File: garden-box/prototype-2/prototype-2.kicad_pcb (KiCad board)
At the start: 2 copper layers, 230 x 150 mm, 23 parts, among them J1 USB_A, J2 Conn_01x03_Male, J3 Conn_01x04_Male, J4 Screw_Terminal_01x02, J5 Screw_Terminal_01x02, J6 Screw_Terminal_01x02, K1 G6DN-1A-L_DC5, Q1 2N3904, T1 Transformer_1P_2S, U1 ESP32-POE

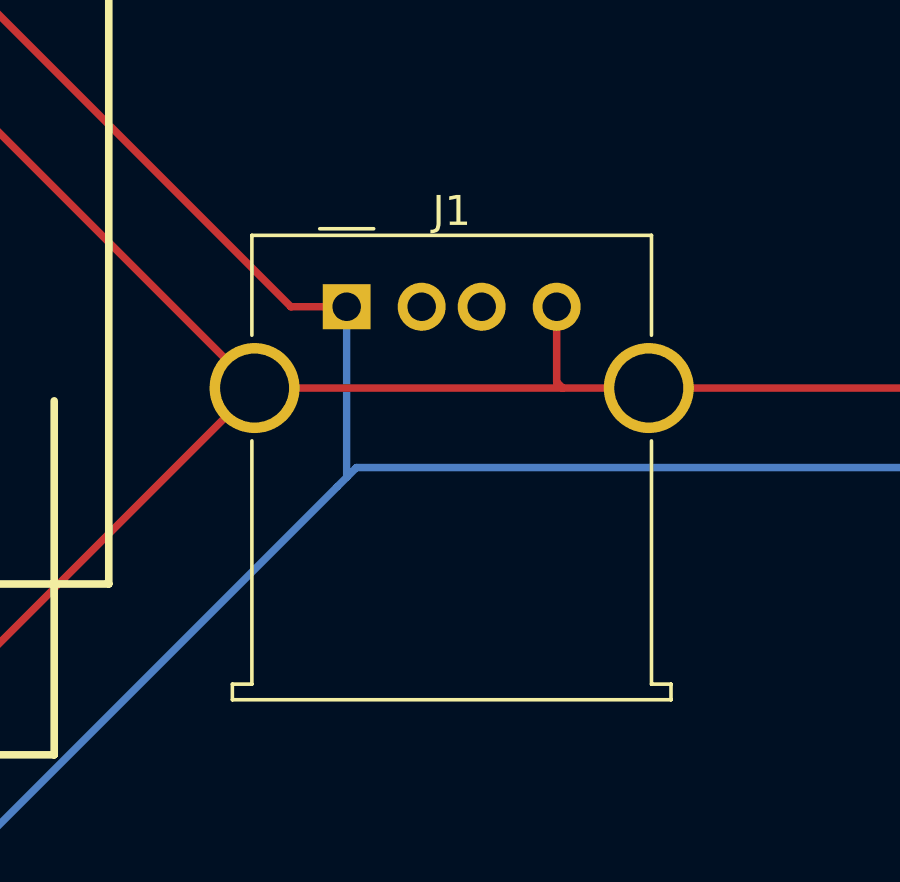
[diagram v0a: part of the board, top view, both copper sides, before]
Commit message: update usb connector
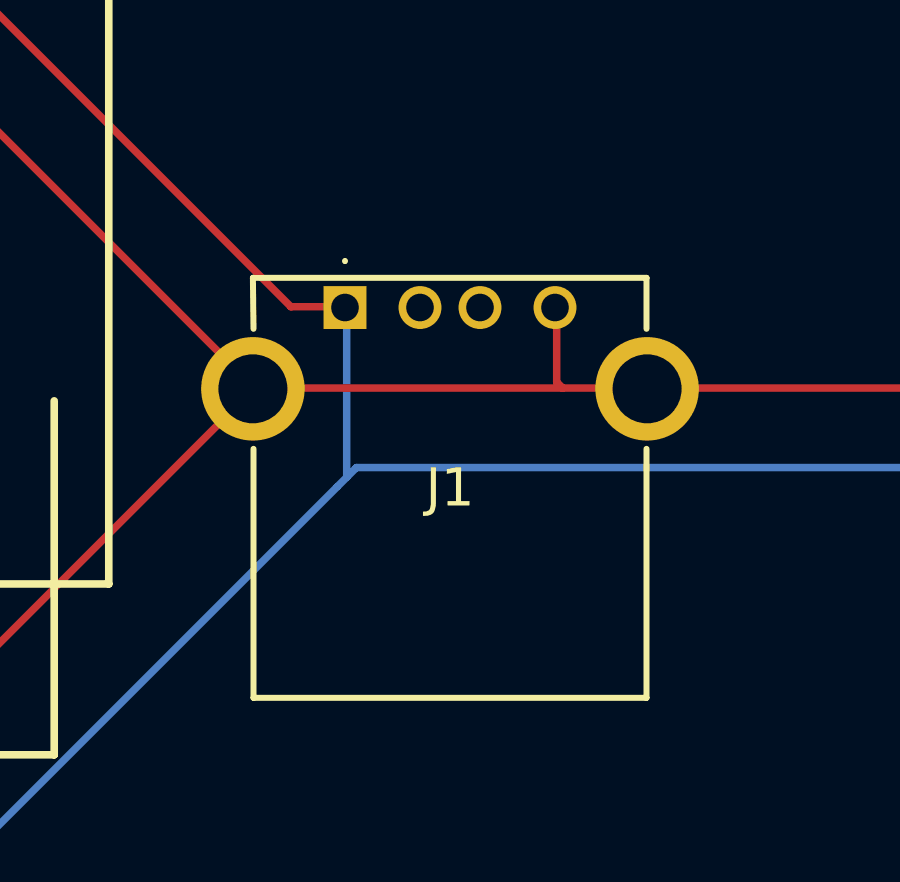
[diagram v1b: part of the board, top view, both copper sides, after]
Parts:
- J1: footprint Connector_USB:USB_A_Molex_67643_Horizontal -> rs-online:875200010BLF
- moved J1 0.06 mm to (159.0, 101.3)
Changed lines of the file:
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@@
-    )
-  )
-  (footprint "Connector_USB:USB_A_Molex_67643_Horizontal" (layer "F.Cu")
-    (at 159.06 101.32)
-    (descr "USB type A, Horizontal, https://www.molex.com/pdm_docs/sd/676433910_sd.pdf")
-    (tags "USB_A Female Connector receptacle")
-    (property "Sheetfile" "prototype-2.kicad_sch")
-    (property "Sheetname" "")
-    (attr through_hole)
-    (fp_text reference "J1" (at 3.5 -3.19) (layer "F.SilkS")
-      (effects (font (size 1 1) (thickness 0.15)))
-    )
-    (fp_text value "USB_A" (at 3.5 14.5) (layer "F.Fab")
-      (effects (font (size 1 1) (thickness 0.15)))
-    )
-    (fp_text user "${REFERENCE}" (at 3.5 3.7) (layer "F.Fab")
-      (effects (font (size 1 1) (thickness 0.15)))
-    )
-    (fp_line (start -3.16 -2.38) (end 10.16 -2.38) (layer "F.SilkS") (width 0.12))
-    (fp_line (start -3.81 12.58) (end -3.81 13.1) (layer "F.SilkS") (width 0.12))
-    (fp_line (start 10.16 4.47) (end 10.16 12.58) (layer "F.SilkS") (width 0.12))
-    (fp_line (start -0.9 -2.6) (end 0.9 -2.6) (layer "F.SilkS") (width 0.12))
-    (fp_line (start -3.16 12.58) (end -3.81 12.58) (layer "F.SilkS") (width 0.12))
-    (fp_line (start -3.16 -2.38) (end -3.16 0.95) (layer "F.SilkS") (width 0.12))
-    (fp_line (start 10.81 12.58) (end 10.16 12.58) (layer "F.SilkS") (width 0.12))
-    (fp_line (start 10.81 13.1) (end 10.81 12.58) (layer "F.SilkS") (width 0.12))
-    (fp_line (start -3.16 12.58) (end -3.16 4.47) (layer "F.SilkS") (width 0.12))
-    (fp_line (start -3.81 13.1) (end 10.81 13.1) (layer "F.SilkS") (width 0.12))
-    (fp_line (start 10.16 -2.38) (end 10.16 0.95) (layer "F.SilkS") (width 0.12))
-    (fp_line (start -4.2 13.49) (end 11.2 13.49) (layer "F.CrtYd") (width 0.05))
-    (fp_line (start -4.2 13.49) (end -4.2 12.19) (layer "F.CrtYd") (width 0.05))
-    (fp_line (start -4.2 12.19) (end -3.55 12.19) (layer "F.CrtYd") (width 0.05))
-    (fp_line (start 10.55 12.19) (end 10.55 4.66) (layer "F.CrtYd") (width 0.05))
-    (fp_line (start 11.2 13.49) (end 11.2 12.19) (layer "F.CrtYd") (width 0.05))
-    (fp_line (start 10.55 -2.77) (end 10.55 0.76) (layer "F.CrtYd") (width 0.05))
-    (fp_line (start 11.2 12.19) (end 10.55 12.19) (layer "F.CrtYd") (width 0.05))
-    (fp_line (start -3.55 -2.77) (end 10.55 -2.77) (layer "F.CrtYd") (width 0.05))
-    (fp_line (start -3.55 12.19) (end -3.55 4.66) (layer "F.CrtYd") (width 0.05))
-    (fp_line (start -3.55 -2.77) (end -3.55 0.76) (layer "F.CrtYd") (width 0.05))
-    (fp_arc (start -3.55 4.66) (mid -5.078208 2.71) (end -3.55 0.76) (layer "F.CrtYd") (width 0.05))
-    (fp_arc (start 10.55 0.76) (mid 12.078208 2.71) (end 10.55 4.66) (layer "F.CrtYd") (width 0.05))
-    (fp_line (start 10.7 12.69) (end 10.05 12.69) (layer "F.Fab") (width 0.1))
-    (fp_line (start -3.7 12.99) (end 10.7 12.99) (layer "F.Fab") (width 0.1))
-    (fp_line (start 10.7 12.99) (end 10.7 12.69) (layer "F.Fab") (width 0.1))
-    (fp_line (start -3.05 12.69) (end -3.05 -2.27) (layer "F.Fab") (width 0.1))
-    (fp_line (start 10.05 -2.27) (end 10.05 12.69) (layer "F.Fab") (width 0.1))
-    (fp_line (start -3.05 12.69) (end -3.7 12.69) (layer "F.Fab") (width 0.1))
-    (fp_line (start -1 -2.27) (end 0 -1.27) (layer "F.Fab") (width 0.1))
-    (fp_line (start -3.05 9.27) (end 10.05 9.27) (layer "F.Fab") (width 0.1))
-    (fp_line (start -3.7 12.69) (end -3.7 12.99) (layer "F.Fab") (width 0.1))
-    (fp_line (start 0 -1.27) (end 1 -2.27) (layer "F.Fab") (width 0.1))
-    (fp_line (start -3.05 -2.27) (end 10.05 -2.27) (layer "F.Fab") (width 0.1))
-    (pad "1" thru_hole rect locked (at 0 0) (size 1.6 1.5) (drill 0.95) (layers *.Cu *.Mask)
-      (net 3 "+5V") (pinfunction "VBUS") (pintype "power_in"))
-    (pad "2" thru_hole circle locked (at 2.5 0) (size 1.6 1.6) (drill 0.95) (layers *.Cu *.Mask)
-      (net 5 "unconnected-(J1-Pad2)") (pinfunction "D-") (pintype "bidirectional"))
-    (pad "3" thru_hole circle locked (at 4.5 0) (size 1.6 1.6) (drill 0.95) (layers *.Cu *.Mask)
-      (net 6 "unconnected-(J1-Pad3)") (pinfunction "D+") (pintype "bidirectional"))
-    (pad "4" thru_hole circle locked (at 7 0) (size 1.6 1.6) (drill 0.95) (layers *.Cu *.Mask)
-      (net 4 "GND") (pinfunction "GND") (pintype "power_in"))
-    (pad "5" thru_hole circle locked (at -3.07 2.71) (size 3 3) (drill 2.3) (layers *.Cu *.Mask)
-      (net 4 "GND") (pinfunction "Shield") (pintype "passive"))
-    (pad "5" thru_hole circle locked (at 10.07 2.71) (size 3 3) (drill 2.3) (layers *.Cu *.Mask)
-      (net 4 "GND") (pinfunction "Shield") (pintype "passive"))
-    (model "${KICAD6_3DMODEL_DIR}/Connector_USB.3dshapes/USB_A_Molex_67643_Horizontal.wrl"
-      (offset (xyz 0 0 0))
-      (scale (xyz 1 1 1))
-      (rotate (xyz 0 0 0))
     )
   )
@@
     )
   )
+  (footprint "rs-online:875200010BLF" (layer "F.Cu")
+    (at 159.004 101.346)
+    (descr "87520-0010BLF-4")
+    (tags "Connector")
+    (property "Sheetfile" "prototype-2.kicad_sch")
+    (property "Sheetname" "")
+    (attr through_hole)
+    (fp_text reference "J1" (at 3.5 6.01) (layer "F.SilkS")
+      (effects (font (size 1.27 1.27) (thickness 0.254)))
+    )
+    (fp_text value "USB_A" (at 3.5 6.01) (layer "F.SilkS") hide
+      (effects (font (size 1.27 1.27) (thickness 0.254)))
+    )
+    (fp_text user "${REFERENCE}" (at 3.5 6.01) (layer "F.Fab")
+      (effects (font (size 1.27 1.27) (thickness 0.254)))
+    )
+    (fp_line (start 10.05 4.71) (end 10.05 13.01) (layer "F.SilkS") (width 0.2))
+    (fp_line (start 0 -1.5) (end 0 -1.5) (layer "F.SilkS") (width 0.1))
+    (fp_line (start -3.05 0.71) (end -3.07 -0.99) (layer "F.SilkS") (width 0.2))
+    (fp_line (start 10.05 13.01) (end -3.05 13.01) (layer "F.SilkS") (width 0.2))
+    (fp_line (start -3.07 -0.99) (end 10.05 -0.99) (layer "F.SilkS") (width 0.2))
+    (fp_line (start -3.05 13.01) (end -3.05 4.71) (layer "F.SilkS") (width 0.2))
+    (fp_line (start 0 -1.6) (end 0 -1.6) (layer "F.SilkS") (width 0.1))
+    (fp_line (start 10.05 -0.99) (end 10.05 0.71) (layer "F.SilkS") (width 0.2))
+    (fp_arc (start 0 -1.5) (mid -0.05 -1.55) (end 0 -1.6) (layer "F.SilkS") (width 0.1))
+    (fp_arc (start 0 -1.6) (mid 0.05 -1.55) (end 0 -1.5) (layer "F.SilkS") (width 0.1))
+    (fp_line (start 12.795 14.01) (end -5.795 14.01) (layer "F.CrtYd") (width 0.1))
+    (fp_line (start -5.795 14.01) (end -5.795 -1.99) (layer "F.CrtYd") (width 0.1))
+    (fp_line (start -5.795 -1.99) (end 12.795 -1.99) (layer "F.CrtYd") (width 0.1))
+    (fp_line (start 12.795 -1.99) (end 12.795 14.01) (layer "F.CrtYd") (width 0.1))
+    (fp_line (start -3.05 13.01) (end 10.05 13.01) (layer "F.Fab") (width 0.1))
+    (fp_line (start 10.05 13.01) (end 10.05 -0.99) (layer "F.Fab") (width 0.1))
+    (fp_line (start 10.05 -0.99) (end -3.05 -0.99) (layer "F.Fab") (width 0.1))
+    (fp_line (start -3.05 -0.99) (end -3.05 13.01) (layer "F.Fab") (width 0.1))
+    (pad "1" thru_hole rect (at 0 0) (size 1.431 1.431) (drill 0.92) (layers *.Cu *.Mask)
+      (net 3 "+5V") (pinfunction "VBUS") (pintype "power_in"))
+    (pad "2" thru_hole circle (at 2.5 0) (size 1.431 1.431) (drill 0.92) (layers *.Cu *.Mask)
+      (net 5 "unconnected-(J1-Pad2)") (pinfunction "D-") (pintype "bidirectional"))
+    (pad "3" thru_hole circle (at 4.5 0) (size 1.431 1.431) (drill 0.92) (layers *.Cu *.Mask)
+      (net 6 "unconnected-(J1-Pad3)") (pinfunction "D+") (pintype "bidirectional"))
+    (pad "4" thru_hole circle (at 7 0) (size 1.431 1.431) (drill 0.92) (layers *.Cu *.Mask)
+      (net 4 "GND") (pinfunction "GND") (pintype "power_in"))
+    (pad "5" thru_hole circle (at 10.07 2.71) (size 3.45 3.45) (drill 2.3) (layers *.Cu *.Mask)
+      (net 4 "GND") (pinfunction "Shield") (pintype "passive"))
+    (pad "5" thru_hole circle (at -3.07 2.71) (size 3.45 3.45) (drill 2.3) (layers *.Cu *.Mask)
+      (net 4 "GND") (pinfunction "Shield") (pintype "passive"))
+    (model "87520-0010BLF.stp"
+      (offset (xyz 3.499999947 0.9899999947 3.449999996))
+      (scale (xyz 1 1 1))
+      (rotate (xyz -90 0 0))
+    )
+  )

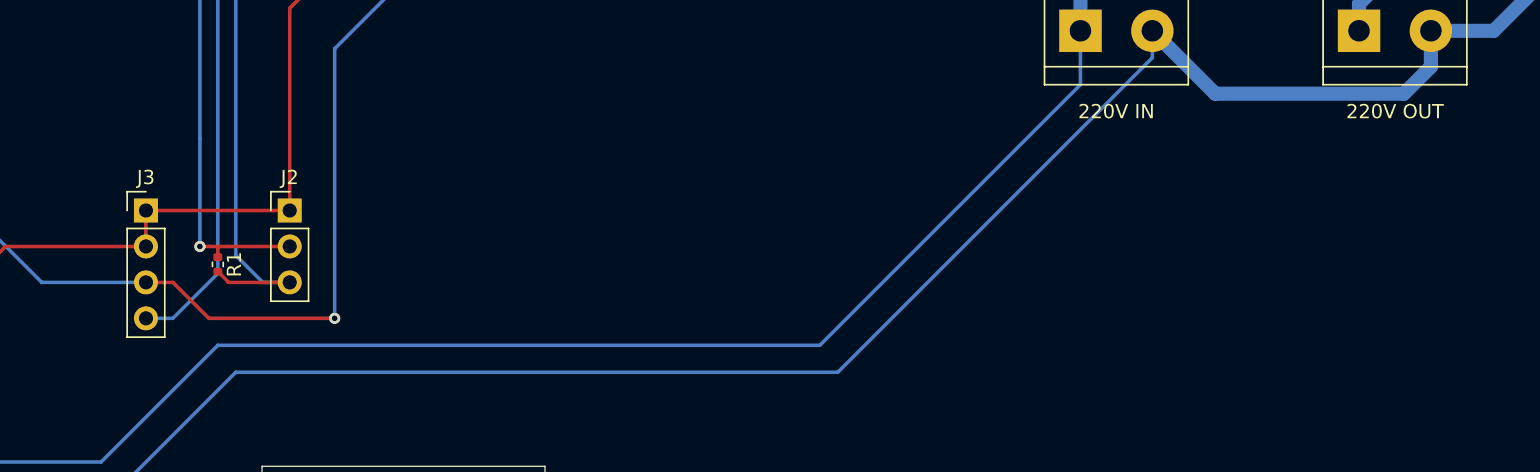
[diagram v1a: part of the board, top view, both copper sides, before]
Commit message: improve silkscreen
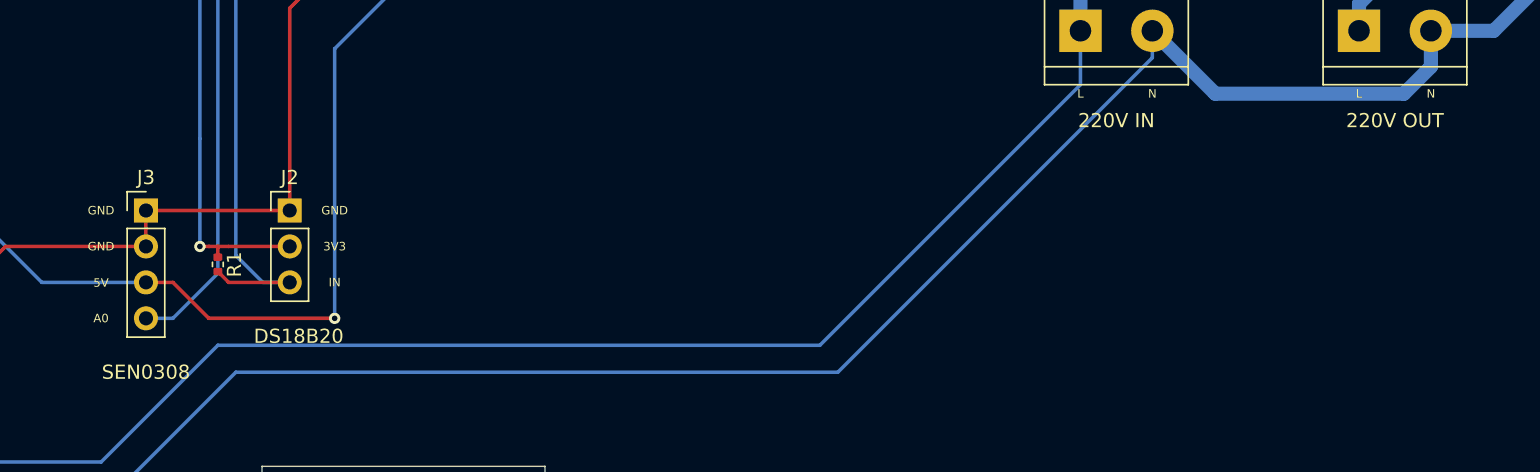
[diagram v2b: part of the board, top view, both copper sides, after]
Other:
- board text added: "3V3"
- board text added: "5V"
- board text added: "A0"
- board text added: "DS18B20"
- board text added: "GND"
- board text added: "IN"
- board text added: "L"
- board text added: "N"
- board text added: "SEN0308"
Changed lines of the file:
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@@
   (gr_line locked (start 39.2 15.24) (end 39.2 33.24) (layer "Edge.Cuts") (width 0.1))
   (gr_line locked (start 30.2 33.24) (end 39.2 33.24) (layer "Edge.Cuts") (width 0.1))
-  (gr_text "220V OUT" (at 215.265 130.175) (layer "F.SilkS")
+  (gr_text "N" (at 217.805 128.905) (layer "F.SilkS")
+    (effects (font (size 0.6 0.6) (thickness 0.125)))
+  )
+  (gr_text "220V OUT" (at 215.265 130.81) (layer "F.SilkS")
     (effects (font (size 1 1) (thickness 0.15)))
   )
@@
     (effects (font (size 1 1) (thickness 0.15)))
   )
+  (gr_text "5V" (at 123.825 142.27) (layer "F.SilkS")
+    (effects (font (size 0.6 0.6) (thickness 0.125)))
+  )
+  (gr_text "GND" (at 140.335 137.16) (layer "F.SilkS")
+    (effects (font (size 0.6 0.6) (thickness 0.125)))
+  )
+  (gr_text "GND" (at 123.825 137.16) (layer "F.SilkS")
+    (effects (font (size 0.6 0.6) (thickness 0.125)))
+  )
+  (gr_text "3V3" (at 140.335 139.7) (layer "F.SilkS")
+    (effects (font (size 0.6 0.6) (thickness 0.125)))
+  )
+  (gr_text "A0" (at 123.825 144.78) (layer "F.SilkS")
+    (effects (font (size 0.6 0.6) (thickness 0.125)))
+  )
+  (gr_text "SEN0308" (at 127 148.59) (layer "F.SilkS")
+    (effects (font (size 1 1) (thickness 0.15)))
+  )
+  (gr_text "L" (at 212.725 128.905) (layer "F.SilkS")
+    (effects (font (size 0.6 0.6) (thickness 0.125)))
+  )
   (gr_text "SWITCH" (at 88.5 72.94) (layer "F.SilkS")
     (effects (font (size 2 2) (thickness 0.3)))
   )
-  (gr_text "220V IN" (at 195.58 130.175) (layer "F.SilkS")
+  (gr_text "N" (at 198.12 128.905) (layer "F.SilkS")
+    (effects (font (size 0.6 0.6) (thickness 0.125)))
+  )
+  (gr_text "L" (at 193.04 128.905) (layer "F.SilkS")
+    (effects (font (size 0.6 0.6) (thickness 0.125)))
+  )
+  (gr_text "DS18B20" (at 137.795 146.05) (layer "F.SilkS")
     (effects (font (size 1 1) (thickness 0.15)))
   )
+  (gr_text "GND" (at 123.825 139.7) (layer "F.SilkS")
+    (effects (font (size 0.6 0.6) (thickness 0.125)))
+  )
+  (gr_text "220V IN" (at 195.58 130.81) (layer "F.SilkS")
+    (effects (font (size 1 1) (thickness 0.15)))
+  )
+  (gr_text "IN" (at 140.335 142.24) (layer "F.SilkS")
+    (effects (font (size 0.6 0.6) (thickness 0.125)))
+  )
   (segment (start 201.295 105.389682) (end 203.220318 105.389682) (width 0.25) (layer "F.Cu") (net 1))

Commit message: change sensor pin
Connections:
- U1 pad 11: unconnected-(U1-Pad11) -> Net-(J2-Pad3)
- U1 pad 18: Net-(J2-Pad3) -> unconnected-(U1-Pad18)
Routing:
- net Net-(J2-Pad3): track 92.3 -> 75.9 mm
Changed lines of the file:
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@@
   (net 23 "unconnected-(U1-Pad9)")
   (net 24 "unconnected-(U1-Pad10)")
-  (net 25 "unconnected-(U1-Pad11)")
+  (net 25 "unconnected-(U1-Pad18)")
   (net 26 "unconnected-(U1-Pad12)")
   (net 27 "unconnected-(U1-Pad13)")
@@
       (net 24 "unconnected-(U1-Pad10)") (pinfunction "GPIO5") (pintype "bidirectional"))
     (pad "11" thru_hole circle (at 12.66 12.83 270) (size 1.778 1.778) (drill 1) (layers *.Cu *.Mask)
-      (net 25 "unconnected-(U1-Pad11)") (pinfunction "GPIO13") (pintype "bidirectional"))
+      (net 8 "Net-(J2-Pad3)") (pinfunction "GPIO13") (pintype "bidirectional"))
     (pad "12" thru_hole circle (at 12.66 10.29 270) (size 1.778 1.778) (drill 1) (layers *.Cu *.Mask)
       (net 26 "unconnected-(U1-Pad12)") (pinfunction "GPIO14") (pintype "bidirectional"))
@@
       (net 30 "unconnected-(U1-Pad17)") (pinfunction "GPIO34") (pintype "no_connect"))
     (pad "18" thru_hole circle (at 12.66 -4.95 270) (size 1.778 1.778) (drill 1) (layers *.Cu *.Mask)
-      (net 8 "Net-(J2-Pad3)") (pinfunction "GPIO35") (pintype "bidirectional"))
+      (net 25 "unconnected-(U1-Pad18)") (pinfunction "GPIO35") (pintype "bidirectional"))
     (pad "19" thru_hole circle (at 12.66 -7.49 270) (size 1.778 1.778) (drill 1) (layers *.Cu *.Mask)
       (net 9 "Net-(J3-Pad4)") (pinfunction "GPIO36") (pintype "bidirectional"))
@@
   (segment (start 132.84 142.24) (end 132.08 141.48) (width 0.25) (layer "F.Cu") (net 8))
   (segment (start 137.16 142.24) (end 132.84 142.24) (width 0.25) (layer "F.Cu") (net 8))
-  (segment (start 143.64 68.71) (end 149.82 68.71) (width 0.25) (layer "B.Cu") (net 8))
-  (segment (start 143.51 68.58) (end 143.64 68.71) (width 0.25) (layer "B.Cu") (net 8))
-  (segment (start 133.35 140.335) (end 133.35 78.74) (width 0.25) (layer "B.Cu") (net 8))
+  (segment (start 133.35 93.98) (end 140.84 86.49) (width 0.25) (layer "B.Cu") (net 8))
+  (segment (start 135.255 142.24) (end 133.35 140.335) (width 0.25) (layer "B.Cu") (net 8))
   (segment (start 137.16 142.24) (end 135.255 142.24) (width 0.25) (layer "B.Cu") (net 8))
-  (segment (start 135.255 142.24) (end 133.35 140.335) (width 0.25) (layer "B.Cu") (net 8))
-  (segment (start 133.35 78.74) (end 143.51 68.58) (width 0.25) (layer "B.Cu") (net 8))
+  (segment (start 140.84 86.49) (end 149.82 86.49) (width 0.25) (layer "B.Cu") (net 8))
+  (segment (start 133.35 140.335) (end 133.35 93.98) (width 0.25) (layer "B.Cu") (net 8))
   (segment (start 144.275 66.17) (end 149.82 66.17) (width 0.25) (layer "B.Cu") (net 9))
   (segment (start 132.08 78.105) (end 144.145 66.04) (width 0.25) (layer "B.Cu") (net 9))

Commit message: placement
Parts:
- added REF**: MountingHole_4.3mm_M4, MountingHole:MountingHole_4.3mm_M4, F.Cu at (143.6, 84.7)
- added REF**: MountingHole_4.3mm_M4, MountingHole:MountingHole_4.3mm_M4, F.Cu at (49.6, 84.7)
- moved J1 106.8 mm to (52.4, 95.0)
- moved J2 91.2 mm to (162.6, 49.5)
- moved J3 91.2 mm to (152.4, 49.5)
- moved R1 91.2 mm to (157.5, 53.3)
- moved U1 62.2 mm to (84.5, 40.6), turned to 90 degrees
- moved PS1 60.7 mm to (73.3, 74.3)
- moved T1 36.9 mm to (191.4, 79.1), turned to 90 degrees
- moved D1 27.6 mm to (198.5, 128.9)
- moved J4 27.6 mm to (185.8, 151.1)
- moved J5 27.6 mm to (205.5, 151.1)
- moved J6 27.6 mm to (223.9, 151.1)
- moved Q1 27.6 mm to (194.0, 130.8)
- moved D2 27.6 mm to (202.3, 129.5)
- moved R2 27.6 mm to (195.6, 127.6)
- moved R3 27.6 mm to (192.8, 127.6)
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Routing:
- net Net-(R2-Pad2): track 66.2 -> 198.1 mm, vias 1 -> 0
- net GND: track 170.2 -> 282.4 mm
- net +5V: track 201.6 -> 266.7 mm, vias 2 -> 1
- net Net-(J6-Pad1): track 68.2 -> 116.8 mm
- net Net-(J4-Pad2): track 304.1 -> 347.0 mm
- net Net-(J5-Pad1): track 127.8 -> 99.8 mm
- net Net-(J6-Pad2): track 105.3 -> 84.3 mm
- net Net-(J3-Pad4): track 92.7 -> 110.3 mm
- net Net-(J2-Pad3): track 75.9 -> 92.0 mm
- net +3V3: track 85.8 -> 96.6 mm
- net Net-(J4-Pad1): track 189.7 -> 196.1 mm
